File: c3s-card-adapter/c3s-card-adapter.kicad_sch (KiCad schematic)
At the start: 2 parts, among them J1 SFM-120-02-L-DH, J2 SFM-120-02-L-DH

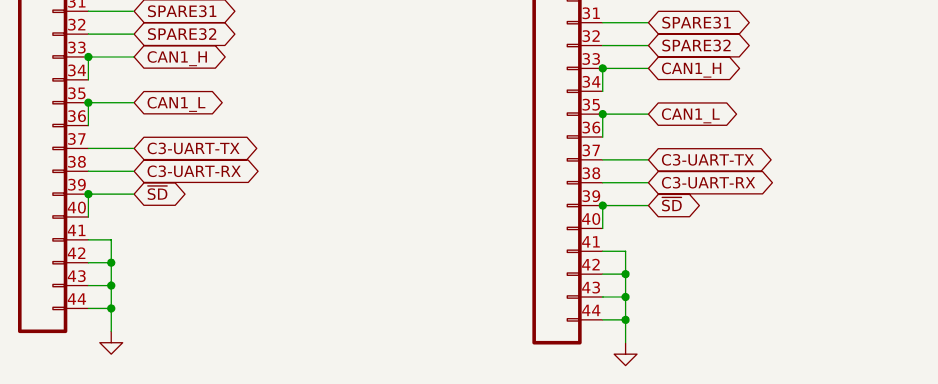
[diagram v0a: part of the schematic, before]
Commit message: Cleanup of v1.0 C3S card adapter. Should be good to go!
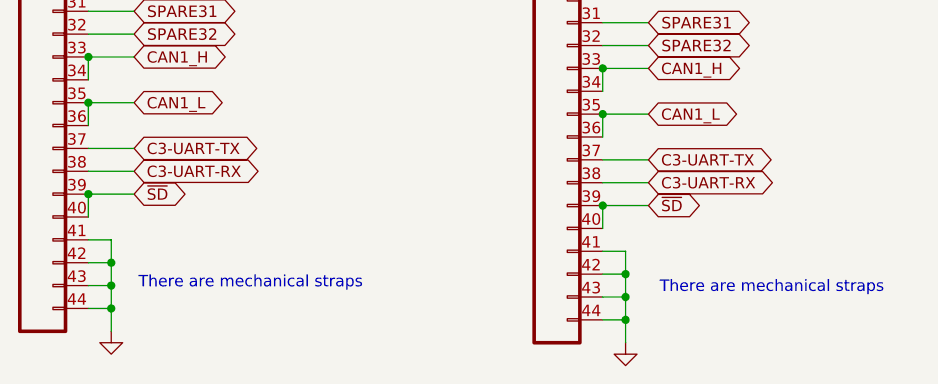
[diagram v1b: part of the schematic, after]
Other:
- note added: "There are mechanical straps"
- title: Flat Sat C3 Surrogate Adapter Board -> C3 Surrogate to OreSat Card Adapter Board

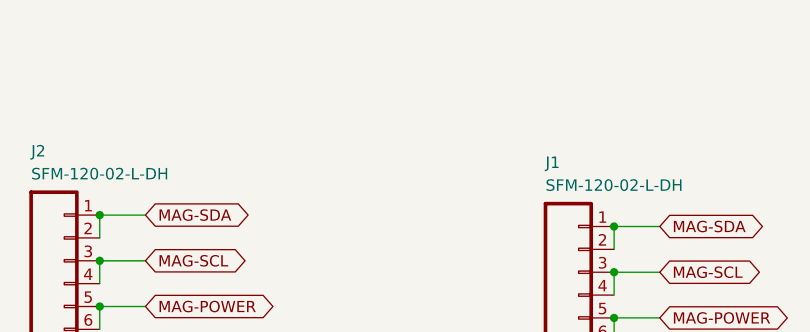
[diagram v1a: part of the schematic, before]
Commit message: Sent v1.0 of the C3S adapter board off to fab!
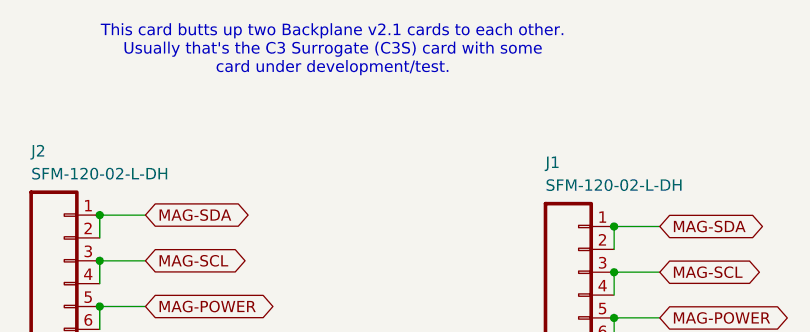
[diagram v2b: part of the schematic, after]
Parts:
- J1, J2: DIS (none) -> DigiKey; DPN (none) -> SAM14509CT-ND; MFR (none) -> Samtec Inc.; MPN (none) -> SFM-120-02-L-DH-TR
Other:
- note added: "This card butts up two Backplane v2.1 cards to each other. Usually that's the C3 Surrogate (C3S) card with some card under development/test."
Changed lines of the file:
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@@
 	(title_block
 		(title "C3 Surrogate to OreSat Card Adapter Board")
-		(date "2026-02-05")
+		(date "2026-03-11")
 		(rev "1.0")
 		(company "Portland State Aerospace Society")
@@
 		(exclude_from_sim no)
 		(at 199.644 188.976 0)
+		(effects
+			(font
+				(size 1.27 1.27)
+			)
+		)
+	)
+	(text "This card butts up two Backplane v2.1 cards to each other. \nUsually that's the C3 Surrogate (C3S) card with some \ncard under development/test."
+		(exclude_from_sim no)
+		(at 207.518 64.262 0)
 		(effects
 			(font
@@
 			)
 		)
-		(property "Datasheet" "https://suddendocs.samtec.com/productspecs/sfm-tfm.pdf"
+		(property "Datasheet" "https://mm.digikey.com/Volume0/opasdata/d220001/medias/docus/6129/sfm-1xx-xx-x-xh-xr-mkt.pdf"
 			(at 176.53 130.81 0)
 			(effects
@@
 			)
 		)
-		(property "Description" ".050\" (1.27 mm) Tiger Eye™ High Reliability Socket and Terminal Strips"
+		(property "Description" "40 Position Receptacle Connector 0.050\" (1.27mm) Surface Mount, Right Angle Gold"
 			(at 176.53 130.81 0)
 			(effects
@@
 			)
 		)
-		(property "DIS" ""
+		(property "DIS" "DigiKey"
 			(at 176.53 130.81 0)
 			(effects
@@
 			)
 		)
-		(property "DPN" ""
+		(property "DPN" "SAM14509CT-ND"
 			(at 176.53 130.81 0)
 			(effects
@@
 			)
 		)
-		(property "MFR" ""
+		(property "MFR" "Samtec Inc."
 			(at 176.53 130.81 0)
 			(effects
@@
 			)
 		)
-		(property "MPN" ""
+		(property "MPN" "SFM-120-02-L-DH-TR"
 			(at 176.53 130.81 0)
 			(effects
@@
 			)
 		)
-		(property "Datasheet" "https://suddendocs.samtec.com/productspecs/sfm-tfm.pdf"
+		(property "Datasheet" "https://mm.digikey.com/Volume0/opasdata/d220001/medias/docus/6129/sfm-1xx-xx-x-xh-xr-mkt.pdf"
 			(at 233.68 132.08 0)
 			(effects
@@
 			)
 		)
-		(property "Description" ".050\" (1.27 mm) Tiger Eye™ High Reliability Socket and Terminal Strips"
+		(property "Description" "40 Position Receptacle Connector 0.050\" (1.27mm) Surface Mount, Right Angle Gold"
 			(at 233.68 132.08 0)
 			(effects
@@
 			)
 		)
-		(property "DIS" ""
+		(property "DIS" "DigiKey"
 			(at 233.68 132.08 0)
 			(effects
@@
 			)
 		)
-		(property "DPN" ""
+		(property "DPN" "SAM14509CT-ND"
 			(at 233.68 132.08 0)
 			(effects
@@
 			)
 		)
-		(property "MFR" ""
+		(property "MFR" "Samtec Inc."
 			(at 233.68 132.08 0)
 			(effects
@@
 			)
 		)
-		(property "MPN" ""
+		(property "MPN" "SFM-120-02-L-DH-TR"
 			(at 233.68 132.08 0)
 			(effects

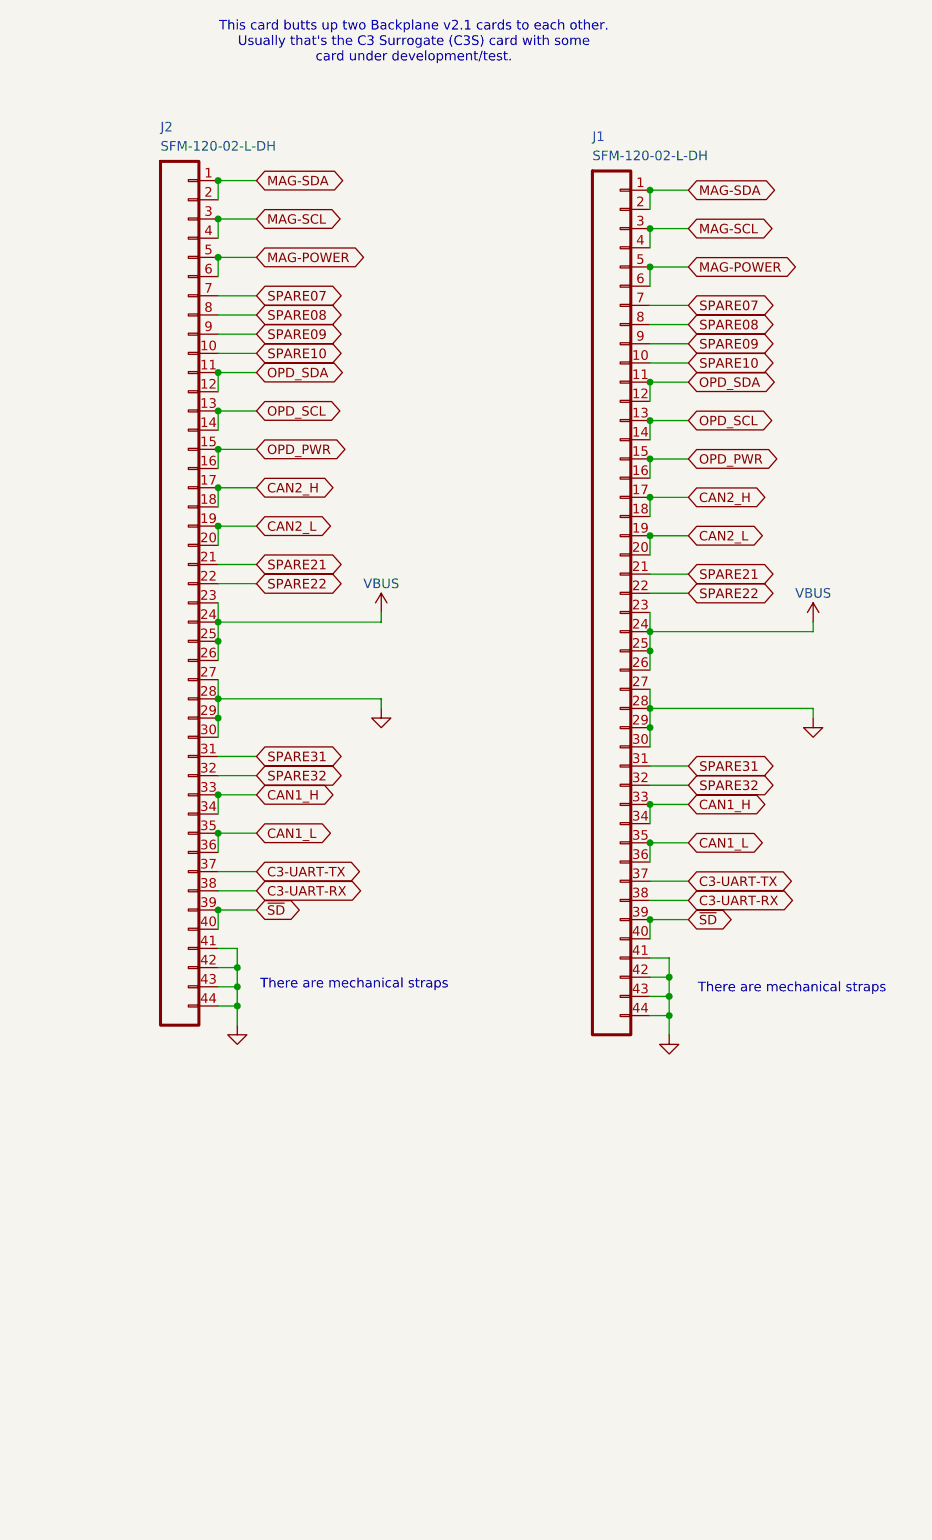
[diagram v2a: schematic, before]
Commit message: C3S adapter board v1.1, now with generic pin-to-pin layout and a connector layout that doesn't crash the PCBs together.
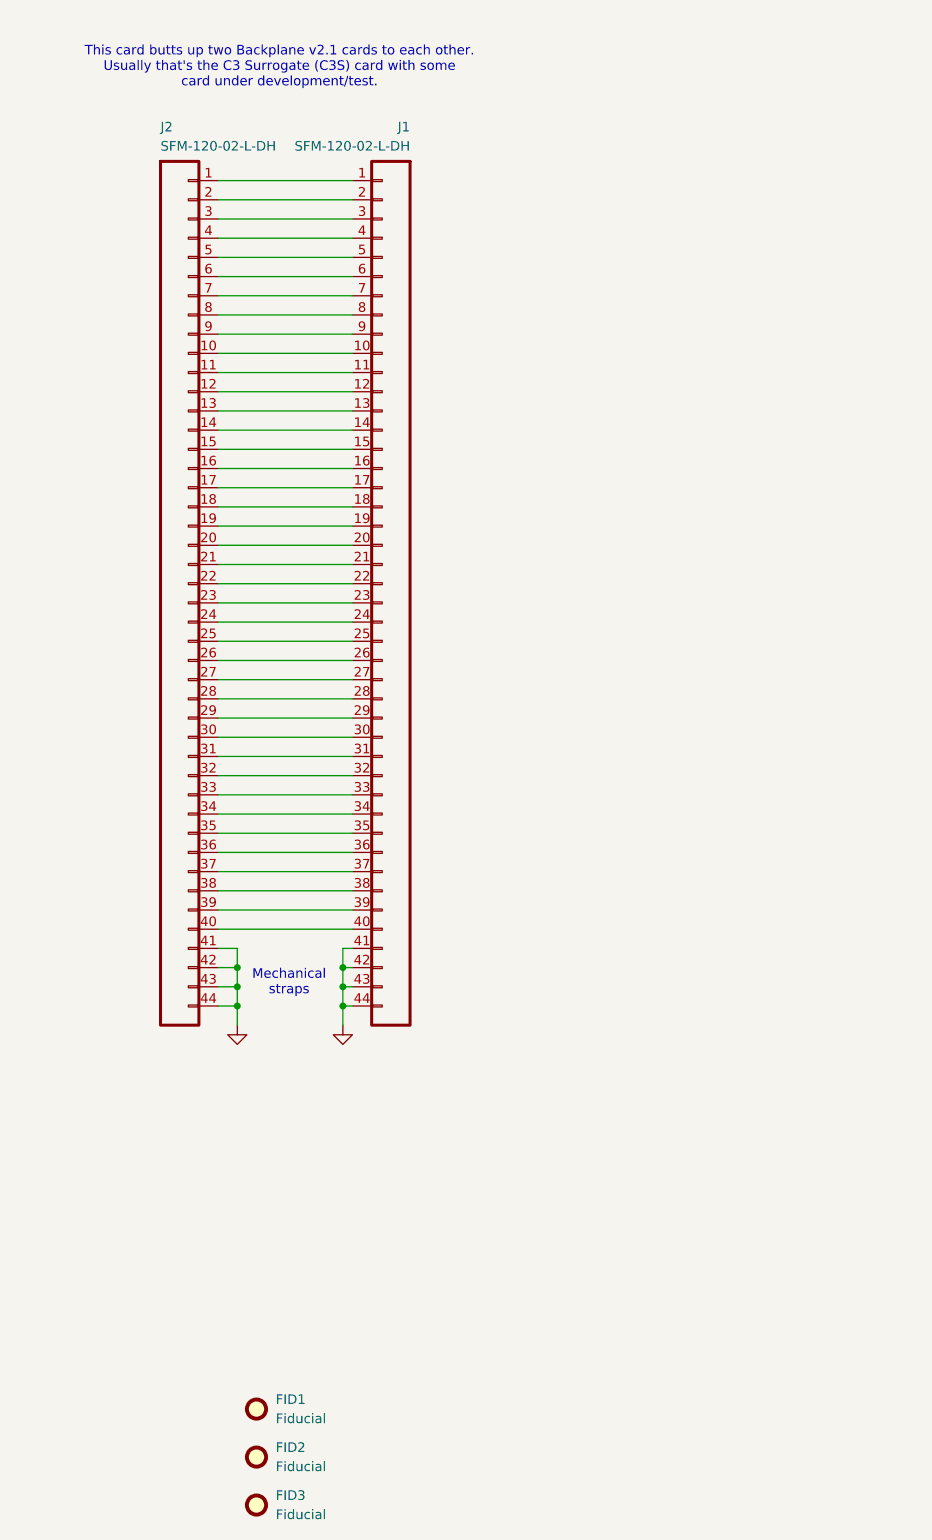
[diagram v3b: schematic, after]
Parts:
- added FID1, FID2, FID3: Fiducial, Fiducial:Fiducial_0.5mm_Mask1mm, symbol Mechanical:Fiducial
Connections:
- net GND: no longer J1.27, J1.28, J1.29, J1.30, J2.27, J2.28, J2.29, J2.30
- net C3-UART-RX: no longer names the net of J1.38, J2.38
- net C3-UART-TX: no longer names the net of J1.37, J2.37
- net CAN1_H: no longer names the net of J1.33, J2.33
- net CAN1_H: no longer J1.34, J2.34
- net CAN1_L: no longer names the net of J1.35, J2.35
- net CAN1_L: no longer J1.36, J2.36
- net CAN2_H: no longer names the net of J1.17, J2.17
- net CAN2_H: no longer J1.18, J2.18
- net CAN2_L: no longer names the net of J1.19, J2.19
- net CAN2_L: no longer J1.20, J2.20
- net MAG-POWER: no longer names the net of J1.5, J2.5
- net MAG-POWER: no longer J1.6, J2.6
- net MAG-SCL: no longer names the net of J1.3, J2.3
- net MAG-SCL: no longer J1.4, J2.4
- net MAG-SDA: no longer names the net of J1.1, J2.1
- net MAG-SDA: no longer J1.2, J2.2
- net OPD_PWR: no longer names the net of J1.15, J2.15
- net OPD_PWR: no longer J1.16, J2.16
- net OPD_SCL: no longer names the net of J1.13, J2.13
- net OPD_SCL: no longer J1.14, J2.14
- net OPD_SDA: no longer names the net of J1.11, J2.11
- net OPD_SDA: no longer J1.12, J2.12
- net SPARE07: no longer names the net of J1.7, J2.7
- net SPARE08: no longer names the net of J1.8, J2.8
- net SPARE09: no longer names the net of J1.9, J2.9
- net SPARE10: no longer names the net of J1.10, J2.10
- net SPARE21: no longer names the net of J1.21, J2.21
- net SPARE22: no longer names the net of J1.22, J2.22
- net SPARE31: no longer names the net of J1.31, J2.31
- net SPARE32: no longer names the net of J1.32, J2.32
- removed net VBUS: J1.23, J1.24, J1.25, J1.26, J2.23, J2.24, J2.25, J2.26
- net ~{SD}: no longer names the net of J1.39, J2.39
- net ~{SD}: no longer J1.40, J2.40
- new net: J1.12, J2.12
- new net: J1.14, J2.14
- new net: J1.16, J2.16
- new net: J1.18, J2.18
- new net: J1.2, J2.2
- new net: J1.20, J2.20
- new net: J1.23, J2.23
- new net: J1.24, J2.24
- new net: J1.25, J2.25
- new net: J1.26, J2.26
- new net: J1.27, J2.27
- new net: J1.28, J2.28
- new net: J1.29, J2.29
- new net: J1.30, J2.30
- new net: J1.34, J2.34
- new net: J1.36, J2.36
- new net: J1.4, J2.4
- new net: J1.40, J2.40
- new net: J1.6, J2.6
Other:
- note added: "Mechanical straps"
- note removed: "There are mechanical straps"
- moved on the sheet: J1
